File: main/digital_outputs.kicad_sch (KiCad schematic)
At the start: 28 parts, among them J10 3.5mm Jack, J11 3.5mm Jack, J8 3.5mm Jack, J9 3.5mm Jack, U16 CD40107, U17 CD40107

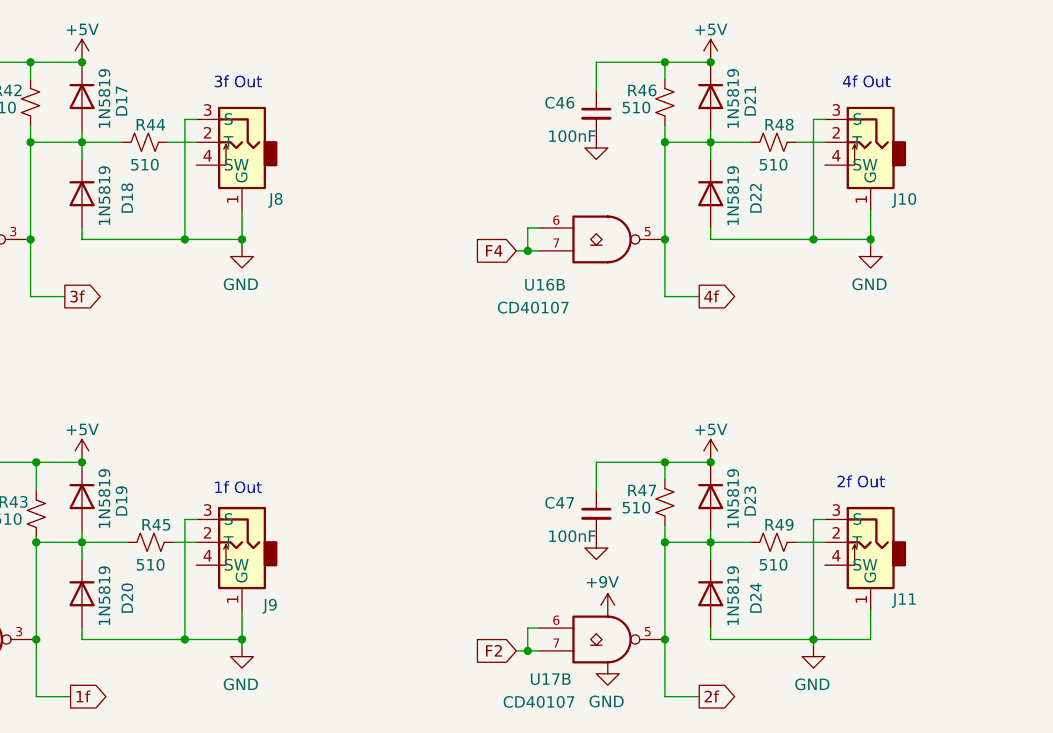
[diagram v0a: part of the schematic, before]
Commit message: Switch to Thonk jacks.
Reduces use of extended parts.
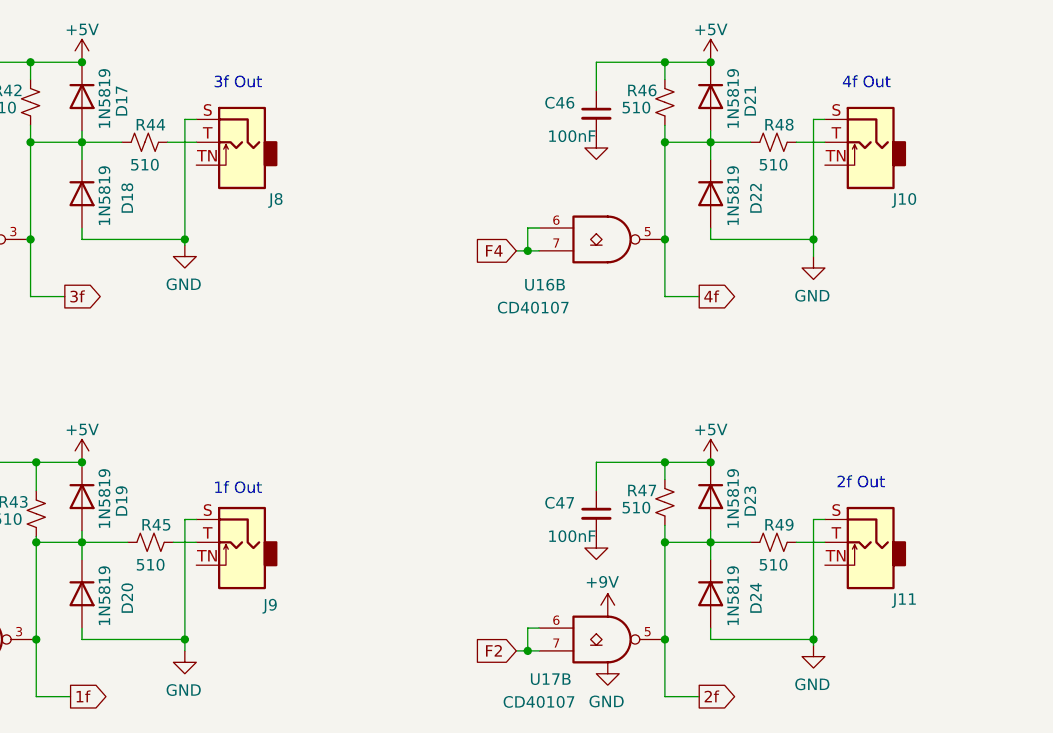
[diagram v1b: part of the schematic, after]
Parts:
- D17, D18, D19, D20, D21, D22, D23, D24: footprint Diode_SMD:D_0805_2012Metric_Pad1.15x1.40mm_HandSolder -> Diode_SMD:D_SOD-323_HandSoldering
- J10, J11, J8, J9: footprint sputterizer:Molex-0472570001 -> audio jacks:Jack_3.5mm_QingPu_WQP-PJ398SM_Vertical; symbol greenface-symbols:Molex_47257 -> Connector:AudioJack2_SwitchT
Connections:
- net GND: now also J10.S, J11.S, J8.S, J9.S; no longer J10.1 (G), J10.3 (S), J11.1 (G), J11.3 (S), J8.1 (G), J8.3 (S), J9.1 (G), J9.3 (S)
- net at R44.1: now also J8.T; no longer J8.2 (T)
- net at R45.1: now also J9.T; no longer J9.2 (T)
- net at R48.1: now also J10.T; no longer J10.2 (T)
- net at R49.1: now also J11.T; no longer J11.2 (T)

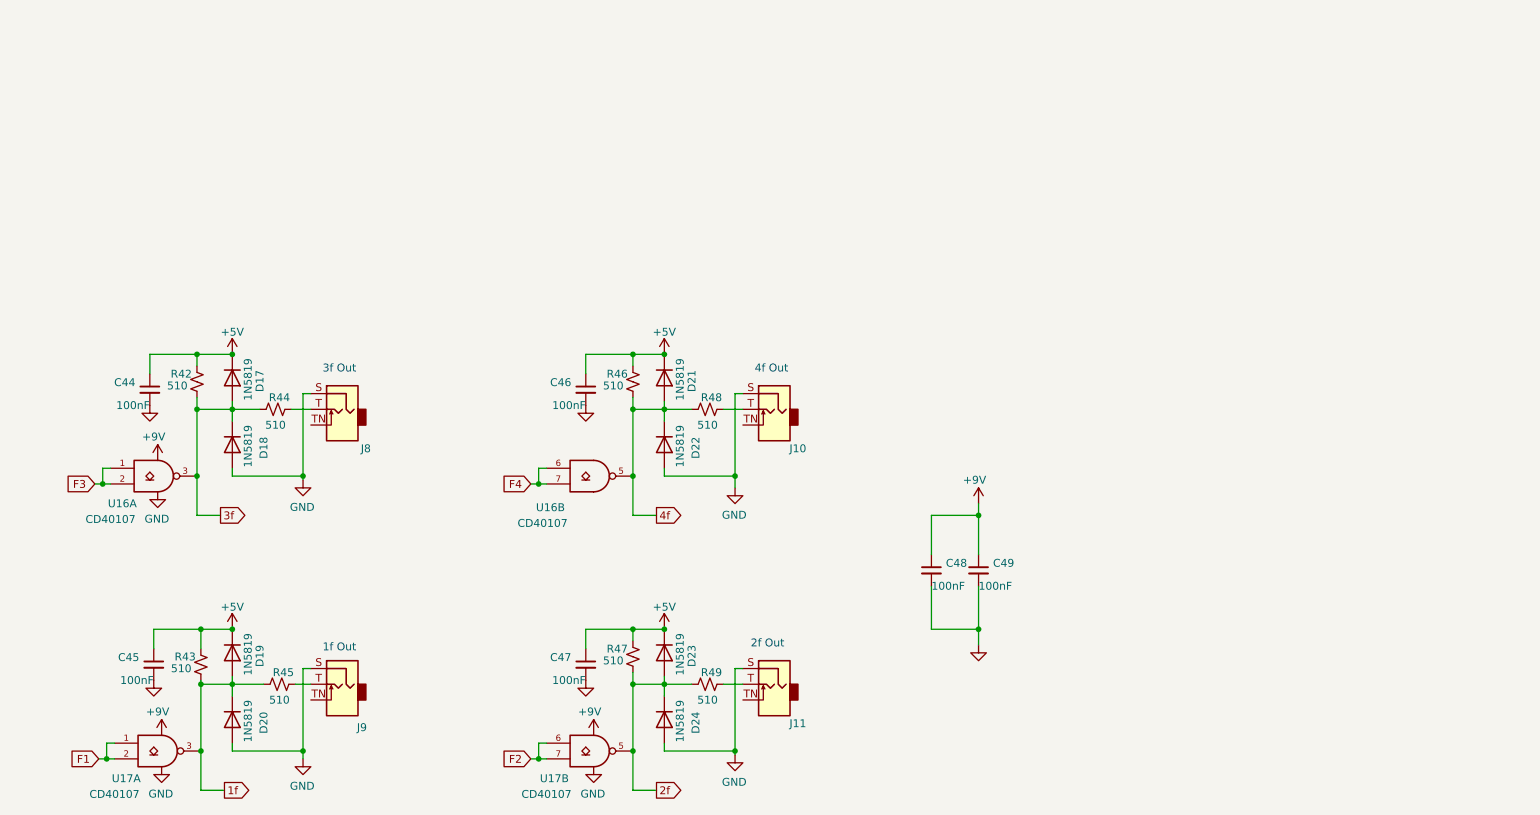
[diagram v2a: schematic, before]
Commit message: Work in progress
Adds User Manual
Changes CV range to 0 - 8V
Adds spice vactrol test circuit.
Adds VCA spice study
Updates other spice and excel files.
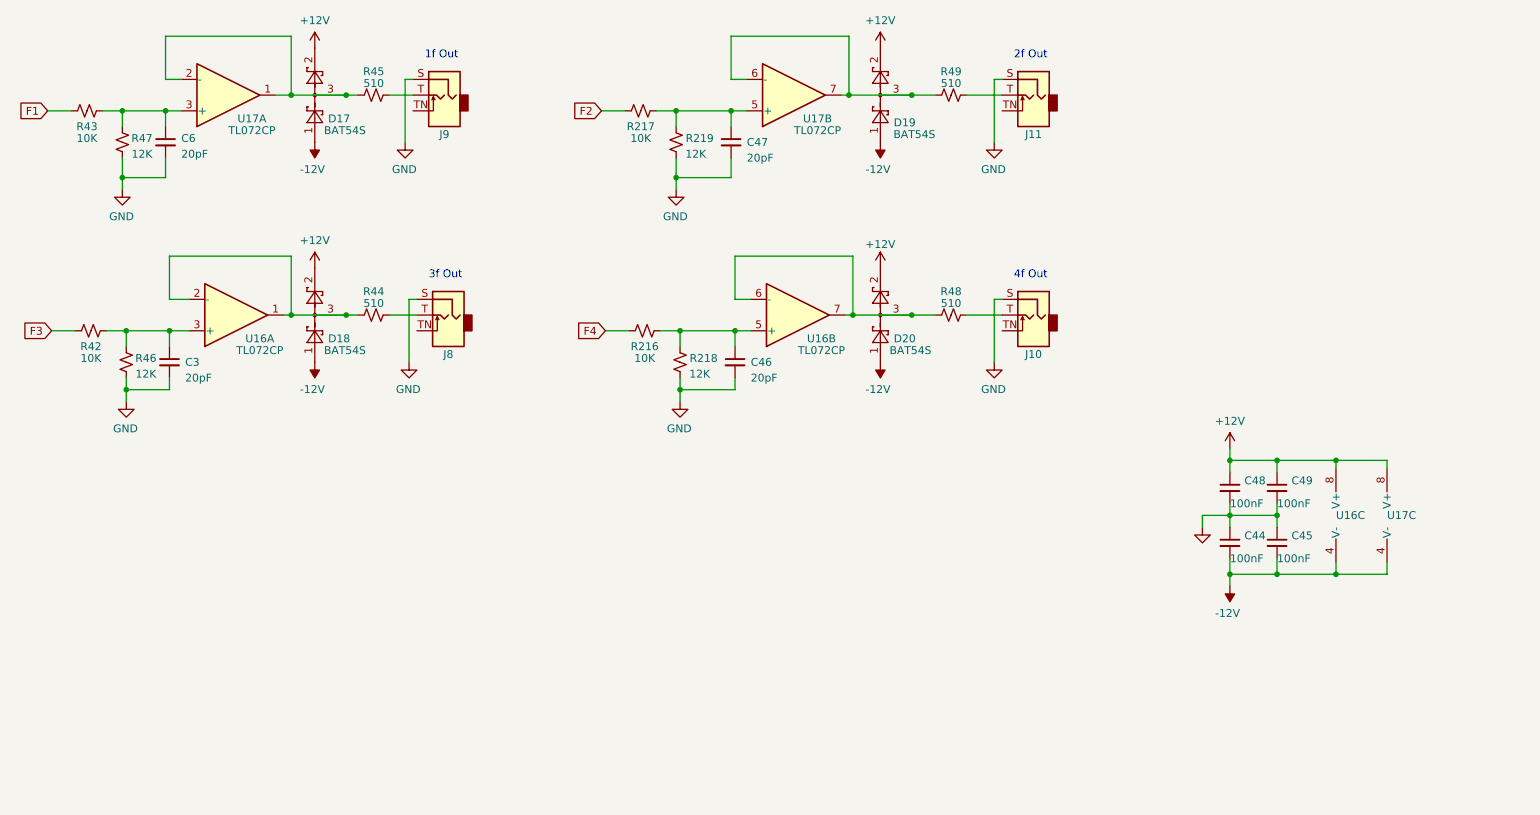
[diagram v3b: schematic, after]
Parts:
- removed D17, D18, D19, D20, D21, D22, D23, D24: 1N5819, Diode_SMD:D_SOD-323_HandSoldering, symbol Diode:1N4148
- removed U16, U17: CD40107, Package_SO:SOIC-8_3.9x4.9mm_P1.27mm, symbol greenface-symbols:CD40107
- added C3, C6: 20pF, Capacitor_SMD:C_0603_1608Metric_Pad1.08x0.95mm_HandSolder, symbol Device:C_Small
- added D17, D18, D19, D20: BAT54S, Package_TO_SOT_SMD:SOT-23, symbol Diode:BAT54S
- added R216, R217: 10K, Resistor_SMD:R_0603_1608Metric, symbol Device:R_Small_US
- added R218, R219: 12K, Resistor_SMD:R_0603_1608Metric, symbol Device:R_Small_US
- added U16, U17: TL072CP, Package_SO:SOIC-8_3.9x4.9mm_P1.27mm, symbol Amplifier_Operational:TL072
- C44, C45, C48, C49: footprint Capacitor_SMD:C_0805_2012Metric_Pad1.18x1.45mm_HandSolder -> Capacitor_SMD:C_0603_1608Metric; LCSC Part # C49678 -> C14663
- C46, C47: value 100nF -> 20pF; footprint Capacitor_SMD:C_0805_2012Metric_Pad1.18x1.45mm_HandSolder -> Capacitor_SMD:C_0603_1608Metric_Pad1.08x0.95mm_HandSolder; Digi-Key Part 478-10836-1-ND -> BC2662CT-ND; LCSC Part # C49678 -> C1648
- R42, R43: value 510 -> 10K; footprint Resistor_SMD:R_0805_2012Metric_Pad1.20x1.40mm_HandSolder -> Resistor_SMD:R_0603_1608Metric; Digi-Key Part PPC470W-1CT-ND -> CRT0805-FZ-1002ELFCT-ND; LCSC Part # C2842425 -> C25804
- R46, R47: value 510 -> 12K; footprint Resistor_SMD:R_0805_2012Metric_Pad1.20x1.40mm_HandSolder -> Resistor_SMD:R_0603_1608Metric; Digi-Key Part PPC470W-1CT-ND -> CRT0805-FZ-1002ELFCT-ND; LCSC Part # C2842425 -> C22790
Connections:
- net F1: now also R43.1
- net F2: now also R217.1
- net F3: now also R42.1
- net F4: now also R216.1
- net GND: now also C44.1, C45.1, R46.2, R47.2, C3.2, C6.2, R218.2, R219.2; no longer C44.2, C45.2
- removed net +5V: C44.1, C45.1, C46.1, C47.1, R42.2, R43.2, R46.2, R47.2
- net +9V renamed +12V
- net +12V: now also D17.2, D18.2, D19.2, D20.2, U16.8 (V+), U17.8 (V+)
- net 1f: no longer names the net of R45.2
- net 1f: now also D17.3, U17.1, U17.2 (-); no longer R43.1
- net 2f: no longer names the net of R47.1
- net 2f: now also R43.2, C6.1, U17.3 (+); no longer R49.2
- net 3f: no longer names the net of R44.2
- net 3f: now also D18.3, U16.1, U16.2 (-); no longer R42.1
- net 4f: no longer names the net of R48.2
- net 4f: now also D20.3, U16.6 (-), U16.7; no longer R46.1
- new net: C47.1, R217.2, R219.1, U17.5 (+)
- new net: C46.1, R216.2, R218.1, U16.5 (+)
- new net: C3.1, R42.2, R46.1, U16.3 (+)
- new net: D19.3, R49.2, U17.6 (-), U17.7
- new net -12V: C44.2, C45.2, D17.1, D18.1, D19.1, D20.1, U16.4 (V-), U17.4 (V-)
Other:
- title: (none) -> Twangilizer
- moved on the sheet: C48, C49, J8, R44

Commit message: v2.0
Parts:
- added C120, C121, C122: 100nF, Capacitor_SMD:C_0603_1608Metric, symbol Device:C_Small
- added D3, D8: BAT54J, Diode_SMD:D_SOD-323F, symbol Diode:BAT54J
- added D4: RED LED, LED_THT:LED_D3.0mm, symbol Device:LED
- added R191: 1M, Resistor_SMD:R_0603_1608Metric, symbol Device:R_Small_US
- added R192, R194, R195: 10K, Resistor_SMD:R_0603_1608Metric, symbol Device:R_Small_US
- added R193: 100K, Resistor_SMD:R_0603_1608Metric, symbol Device:R_Small_US
- added R196: 10.7K, Resistor_SMD:R_0603_1608Metric, symbol Device:R_Small_US
- added U47: TL072CP, Package_SO:SOIC-8_3.9x4.9mm_P1.27mm, symbol Amplifier_Operational:TL072
- J10, J11, J8, J9: footprint audio jacks:Jack_3.5mm_QingPu_WQP-PJ398SM_Vertical -> greenface:Jack_3.5mm_QingPu_WQP-PJ398SM_Vertical
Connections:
- net +12V: now also C121.1, R192.1, U47.8 (V+)
- net -12V: now also C122.2, U47.4 (V-)
- net GND: now also C121.2, C122.1, R195.1
- new net: D3.1 (K), R195.2, U47.5 (+)
- new net: D8.2 (A), R194.1
- new net: R194.2, R196.1, U47.6 (-)
- new net: C120.2, R193.1
- new net: D4.1 (K), R193.2, U47.1
- new net: D4.2 (A), R192.2
- new net: C120.1, R191.1, U47.3 (+)
- new net: R196.2, U47.2 (-), U47.7
- new net +9V: R191.2
- new net SIG: D3.2 (A), D8.1 (K)
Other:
- note added: "Clip Detector"
- moved on the sheet: U16C, U17C
